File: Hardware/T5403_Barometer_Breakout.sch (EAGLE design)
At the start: 16 parts, among them U1 T5400

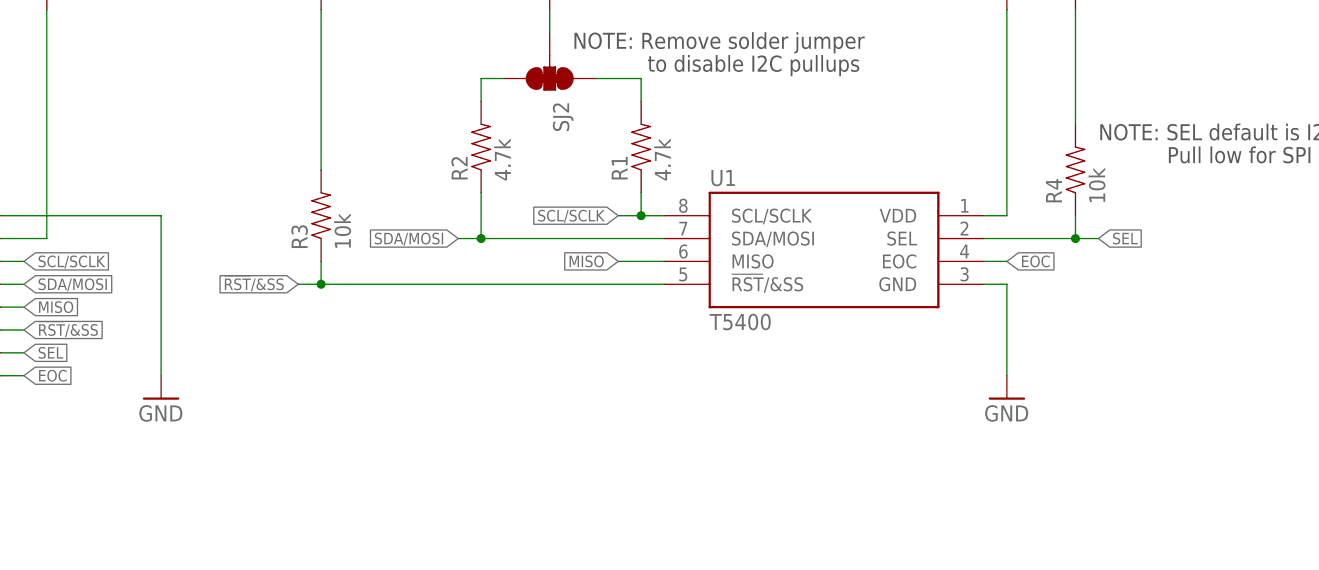
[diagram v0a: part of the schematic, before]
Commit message: cleaned up SCH and replaced components with correct Sparkle ID's
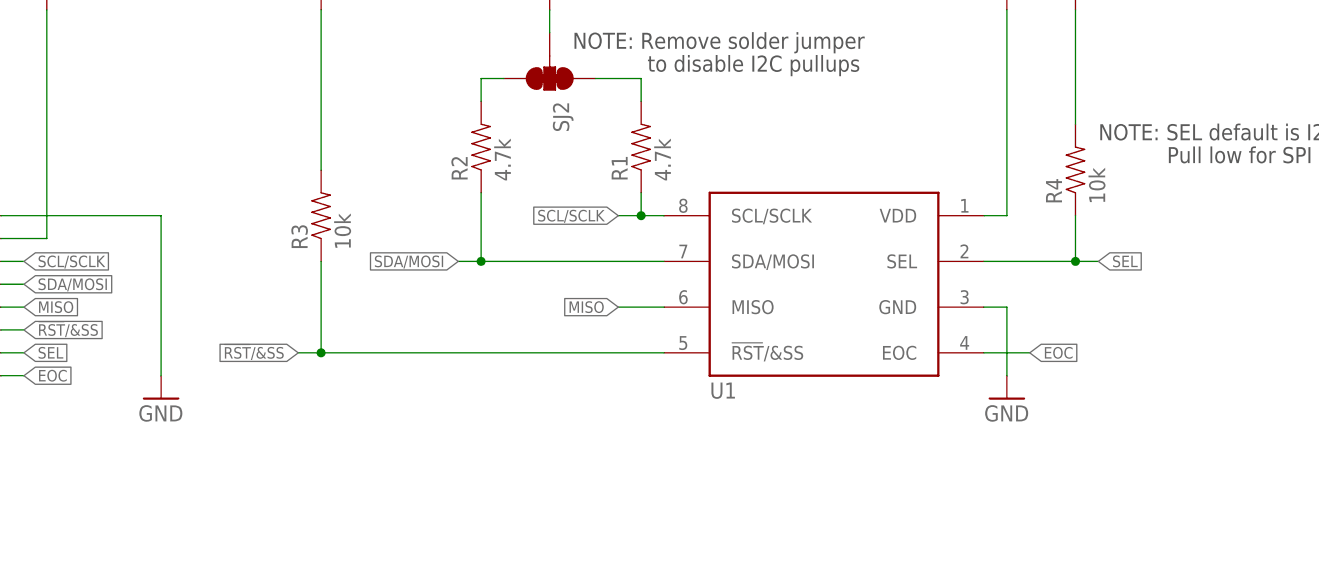
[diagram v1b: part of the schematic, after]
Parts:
- R1, R2: device SparkFun-Passives:RESISTOR0603-RES -> SparkFun-Resistors:4.7KOHM1/10W1%(0603)
- R3, R4: device SparkFun-Passives:RESISTOR0603-RES -> SparkFun-Resistors:10KOHM1/10W1%(0603)0603
- U1: device T5400:T5400 -> SparkFun-Sensors:T5400
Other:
- moved on the sheet: U1
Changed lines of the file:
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@@
 <?xml version="1.0" encoding="utf-8"?>
 <!DOCTYPE eagle SYSTEM "eagle.dtd">
-<eagle version="6.0">
+<eagle version="6.5.0">
 <drawing>
 <settings>
@@
 </classes>
 <parts>
-<part name="U1" library="T5400" deviceset="T5400" device=""/>
+<part name="U1" library="SparkFun-Sensors" deviceset="T5400" device=""/>
 <part name="JP1" library="SparkFun-Connectors" deviceset="M08" device="1X08"/>
 <part name="GND1" library="SparkFun-Aesthetics" deviceset="GND" device=""/>
 <part name="FRAME1" library="SparkFun-Aesthetics" deviceset="FRAME-LETTER" device="" value="FRAME-LETTER"/>
 <part name="LOGO2" library="SparkFun-Aesthetics" deviceset="OSHW-LOGO" device="S"/>
-<part name="R1" library="SparkFun-Passives" deviceset="RESISTOR" device="0603-RES" value="4.7k"/>
-<part name="R2" library="SparkFun-Passives" deviceset="RESISTOR" device="0603-RES" value="4.7k"/>
+<part name="R1" library="SparkFun-Resistors" deviceset="4.7KOHM1/10W1%(0603)" device="" value="4.7k"/>
+<part name="R2" library="SparkFun-Resistors" deviceset="4.7KOHM1/10W1%(0603)" device="" value="4.7k"/>
 <part name="SUPPLY1" library="SparkFun-Aesthetics" deviceset="VCC" device=""/>
 <part name="C1" library="SparkFun-Capacitors" deviceset="0.1UF-25V-5%(0603)" device="" value=".1uF"/>
@@
 <part name="STANDOFF2" library="SparkFun-Electromechanical" deviceset="STAND-OFF" device=""/>
 <part name="LOGO1" library="SparkFun-Aesthetics" deviceset="LOGO-SFE" device="NEW"/>
-<part name="R3" library="SparkFun-Passives" deviceset="RESISTOR" device="0603-RES" value="10k"/>
+<part name="R3" library="SparkFun-Resistors" deviceset="10KOHM1/10W1%(0603)" device="0603" value="10k"/>
 <part name="SUPPLY6" library="SparkFun-Aesthetics" deviceset="VCC" device=""/>
 <part name="FID1" library="SparkFun-Aesthetics" deviceset="FIDUCIAL" device="1X2"/>
@@
 <part name="SJ2" library="SparkFun-Passives" deviceset="SOLDERJUMPER_2WAY" device="PASTE1&amp;2&amp;3"/>
 <part name="SUPPLY2" library="SparkFun-Aesthetics" deviceset="VCC" device=""/>
-<part name="R4" library="SparkFun-Passives" deviceset="RESISTOR" device="0603-RES" value="10k"/>
+<part name="R4" library="SparkFun-Resistors" deviceset="10KOHM1/10W1%(0603)" device="0603" value="10k"/>
 <part name="SUPPLY3" library="SparkFun-Aesthetics" deviceset="VCC" device=""/>
 </parts>
@@
 <pinref part="U1" gate="U$1" pin="GND"/>
 <pinref part="GND1" gate="1" pin="GND"/>
-<wire x1="175.26" y1="81.28" x2="175.26" y2="91.44" width="0.1524" layer="91"/>
-<wire x1="175.26" y1="91.44" x2="172.72" y2="91.44" width="0.1524" layer="91"/>
+<wire x1="175.26" y1="81.28" x2="175.26" y2="88.9" width="0.1524" layer="91"/>
+<wire x1="175.26" y1="88.9" x2="172.72" y2="88.9" width="0.1524" layer="91"/>
 </segment>
 <segment>
@@
 <segment>
 <pinref part="U1" gate="U$1" pin="SEL"/>
-<wire x1="172.72" y1="96.52" x2="182.88" y2="96.52" width="0.1524" layer="91"/>
-<label x="185.42" y="96.52" size="1.27" layer="95" xref="yes"/>
+<wire x1="172.72" y1="93.98" x2="182.88" y2="93.98" width="0.1524" layer="91"/>
+<label x="185.42" y="93.98" size="1.27" layer="95" xref="yes"/>
 <pinref part="R4" gate="G$1" pin="1"/>
-<wire x1="182.88" y1="96.52" x2="185.42" y2="96.52" width="0.1524" layer="91"/>
-<wire x1="182.88" y1="99.06" x2="182.88" y2="96.52" width="0.1524" layer="91"/>
-<junction x="182.88" y="96.52"/>
+<wire x1="182.88" y1="93.98" x2="185.42" y2="93.98" width="0.1524" layer="91"/>
+<wire x1="182.88" y1="99.06" x2="182.88" y2="93.98" width="0.1524" layer="91"/>
+<junction x="182.88" y="93.98"/>
 </segment>
 <segment>
@@
 <segment>
 <pinref part="U1" gate="U$1" pin="EOC"/>
-<wire x1="172.72" y1="93.98" x2="175.26" y2="93.98" width="0.1524" layer="91"/>
-<label x="175.26" y="93.98" size="1.27" layer="95" xref="yes"/>
+<wire x1="172.72" y1="83.82" x2="177.8" y2="83.82" width="0.1524" layer="91"/>
+<label x="177.8" y="83.82" size="1.27" layer="95" xref="yes"/>
 </segment>
 <segment>
@@
 <pinref part="U1" gate="U$1" pin="!RST!/&amp;SS"/>
 <pinref part="R3" gate="G$1" pin="1"/>
-<label x="96.52" y="91.44" size="1.27" layer="95" rot="R180" xref="yes"/>
-<wire x1="96.52" y1="91.44" x2="99.06" y2="91.44" width="0.1524" layer="91"/>
-<wire x1="99.06" y1="91.44" x2="99.06" y2="93.98" width="0.1524" layer="91"/>
-<wire x1="99.06" y1="91.44" x2="137.16" y2="91.44" width="0.1524" layer="91"/>
-<junction x="99.06" y="91.44"/>
+<label x="96.52" y="83.82" size="1.27" layer="95" rot="R180" xref="yes"/>
+<wire x1="96.52" y1="83.82" x2="99.06" y2="83.82" width="0.1524" layer="91"/>
+<wire x1="99.06" y1="83.82" x2="99.06" y2="93.98" width="0.1524" layer="91"/>
+<wire x1="99.06" y1="83.82" x2="137.16" y2="83.82" width="0.1524" layer="91"/>
+<junction x="99.06" y="83.82"/>
 </segment>
 <segment>
@@
 <segment>
 <pinref part="U1" gate="U$1" pin="MISO"/>
-<wire x1="137.16" y1="93.98" x2="132.08" y2="93.98" width="0.1524" layer="91"/>
-<label x="132.08" y="93.98" size="1.27" layer="95" rot="R180" xref="yes"/>
+<wire x1="137.16" y1="88.9" x2="132.08" y2="88.9" width="0.1524" layer="91"/>
+<label x="132.08" y="88.9" size="1.27" layer="95" rot="R180" xref="yes"/>
 </segment>
 <segment>
@@
 <segment>
 <pinref part="U1" gate="U$1" pin="SDA/MOSI"/>
-<wire x1="137.16" y1="96.52" x2="116.84" y2="96.52" width="0.1524" layer="91"/>
+<wire x1="137.16" y1="93.98" x2="116.84" y2="93.98" width="0.1524" layer="91"/>
 <pinref part="R2" gate="G$1" pin="1"/>
-<wire x1="116.84" y1="96.52" x2="116.84" y2="101.6" width="0.1524" layer="91"/>
-<label x="114.3" y="96.52" size="1.27" layer="95" rot="R180" xref="yes"/>
-<wire x1="114.3" y1="96.52" x2="116.84" y2="96.52" width="0.1524" layer="91"/>
-<junction x="116.84" y="96.52"/>
-</segment>
-<segment>
+<wire x1="116.84" y1="93.98" x2="116.84" y2="101.6" width="0.1524" layer="91"/>
+<label x="114.3" y="93.98" size="1.27" layer="95" rot="R180" xref="yes"/>
+<wire x1="114.3" y1="93.98" x2="116.84" y2="93.98" width="0.1524" layer="91"/>
+<junction x="116.84" y="93.98"/>
+</segment>
+<segment>
